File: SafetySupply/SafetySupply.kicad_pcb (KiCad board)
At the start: 2 copper layers, 30 x 60 mm, 48 parts, among them J1 Screw_Terminal_01x02, J2 Conn_01x01, J3 Screw_Terminal_01x02, J4 Conn_01x01, J5 Screw_Terminal_01x02, J6 Conn_01x01, J7 Conn_01x01, J8 Conn_01x01, J9 Conn_01x01, K1 FRM18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

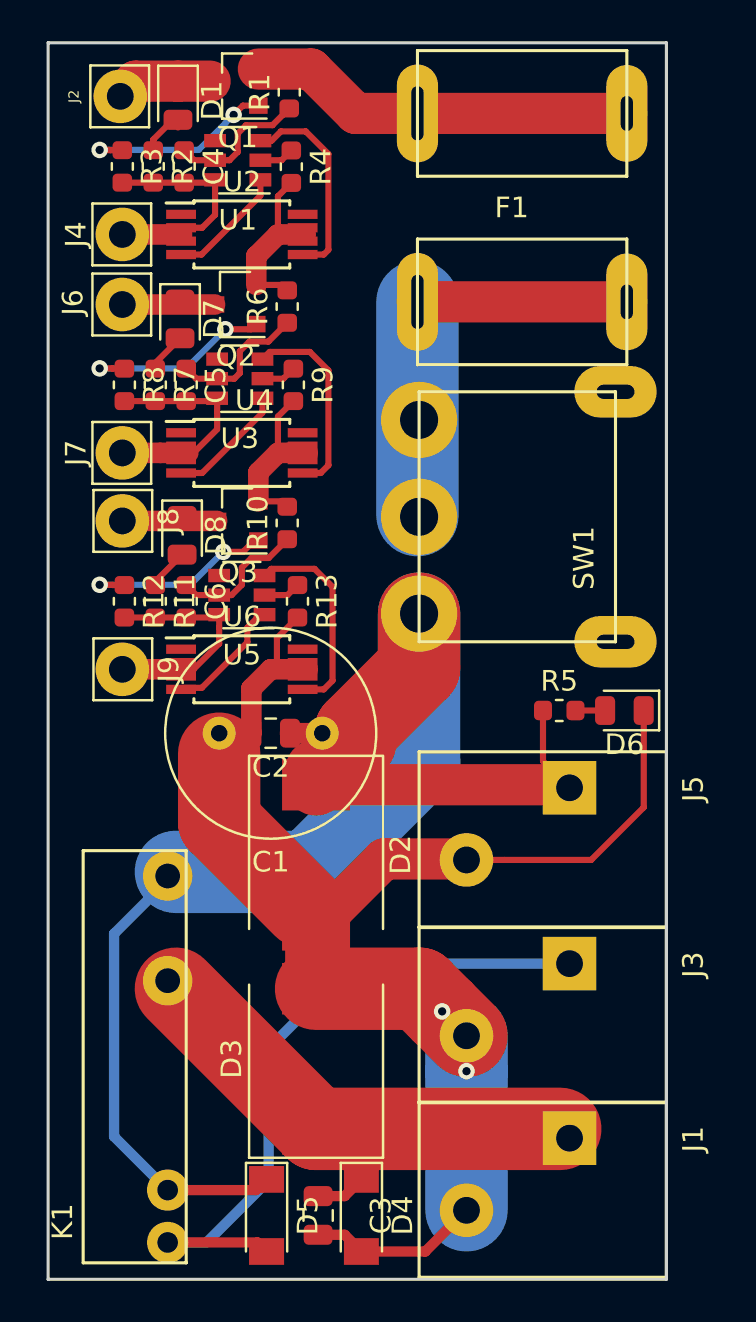
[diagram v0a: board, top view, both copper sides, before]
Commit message: Fixed silkscreen for SafetySupply, added mounting holes.
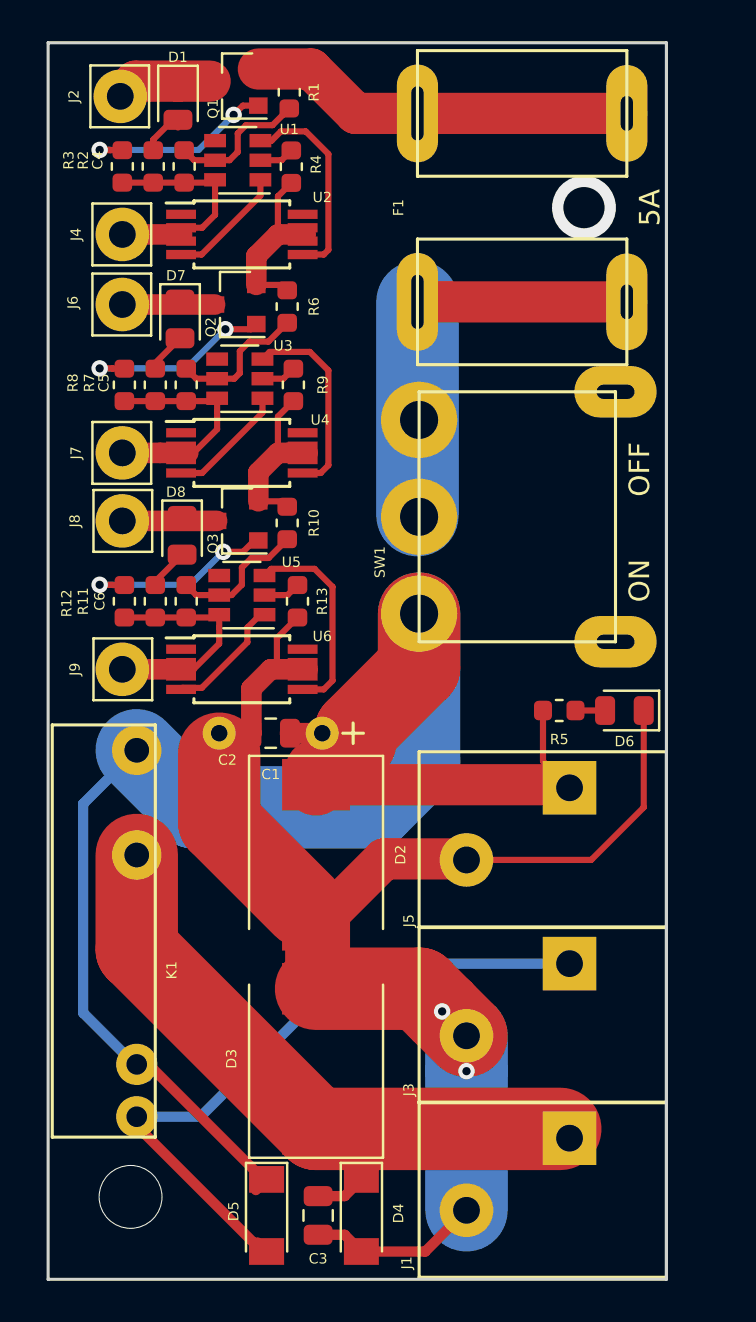
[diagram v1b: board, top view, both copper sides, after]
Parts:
- C1: footprint Capacitor_THT:C_Radial_D10.0mm_H20.0mm_P5.00mm -> Footprints:C_Radial_D10.0mm_H20.0mm_P5.00mm
- moved K1 6.28 mm to (138.2, 104.1)
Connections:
- SW1 pad 0: (no net) -> GND
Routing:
- net Net-(C3-Pad1): track 27.0 -> 34.2 mm
- net +12V: track 70.8 -> 76.4 mm
- net (no net): vias 0 -> 2
- added copper zone on B.Cu, net GND
- added copper zone on F.Cu, net GND
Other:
- board text added: "5A"
- board text added: "OFF"
- board text added: "ON"

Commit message: Added grouding vias in SafetySupply.
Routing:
- net GND: vias 2 -> 13
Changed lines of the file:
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@@
     (thickness 1.6)
     (drawings 7)
-    (tracks 226)
+    (tracks 237)
     (zones 0)
     (modules 48)
@@
   )
   (setup
-    (last_trace_width 0.5)
+    (last_trace_width 0.25)
     (user_trace_width 0.3)
     (user_trace_width 0.5)
@@
   (segment (start 153.018 106.9) (end 148 106.9) (width 4) (layer F.Cu) (net 7))
   (segment (start 155.3 110.9) (end 155.3 109.182) (width 4) (layer B.Cu) (net 7))
-  (via (at 155.3 110.9) (size 0.8) (drill 0.4) (layers F.Cu B.Cu) (net 7))
   (segment (start 154.118 108) (end 155.3 109.182) (width 4) (layer F.Cu) (net 7))
-  (via (at 154.118 108) (size 0.8) (drill 0.4) (layers F.Cu B.Cu) (net 7))
+  (via (at 162 118) (size 0.8) (drill 0.4) (layers F.Cu B.Cu) (net 7))
+  (via (at 162 110) (size 0.8) (drill 0.4) (layers F.Cu B.Cu) (net 7))
+  (via (at 162 102) (size 0.8) (drill 0.4) (layers F.Cu B.Cu) (net 7))
+  (via (at 162 86) (size 0.8) (drill 0.4) (layers F.Cu B.Cu) (net 7))
+  (via (at 162 81) (size 0.8) (drill 0.4) (layers F.Cu B.Cu) (net 7))
+  (via (at 157 69) (size 0.8) (drill 0.4) (layers F.Cu B.Cu) (net 7))
+  (via (at 151 69) (size 0.8) (drill 0.4) (layers F.Cu B.Cu) (net 7))
+  (via (at 137 68) (size 0.8) (drill 0.4) (layers F.Cu B.Cu) (net 7))
+  (via (at 137 79) (size 0.8) (drill 0.4) (layers F.Cu B.Cu) (net 7))
+  (via (at 137 89) (size 0.8) (drill 0.4) (layers F.Cu B.Cu) (net 7))
+  (via (at 144 104) (size 0.8) (drill 0.4) (layers F.Cu B.Cu) (net 7))
+  (via (at 142 119) (size 0.8) (drill 0.4) (layers F.Cu B.Cu) (net 7))
+  (via (at 137 114) (size 0.8) (drill 0.4) (layers F.Cu B.Cu) (net 7))
   (segment (start 146.6125 87.8) (end 145.5 87.8) (width 0.3) (layer F.Cu) (net 8))
   (segment (start 147.1 87.3125) (end 146.6125 87.8) (width 0.3) (layer F.Cu) (net 8))

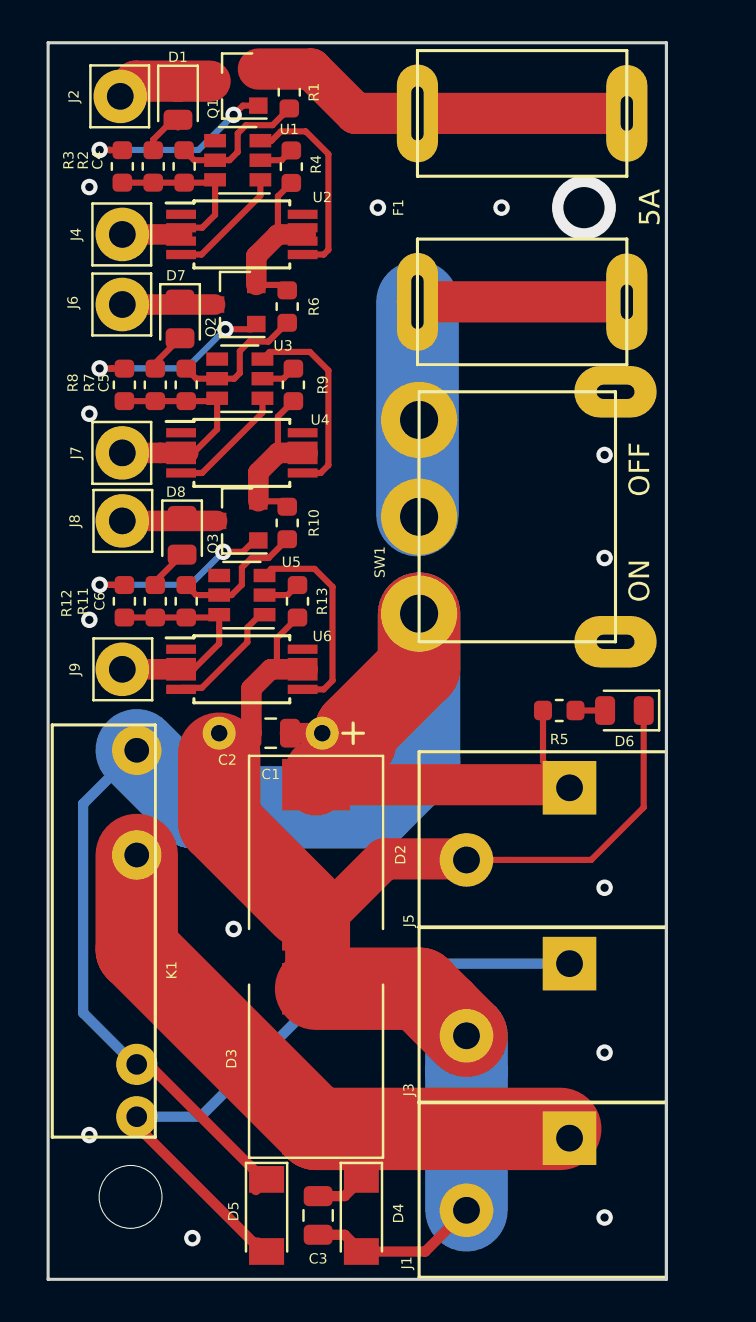
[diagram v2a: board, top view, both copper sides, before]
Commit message: First review. Fixed polygon pours, silkscreen and soldermask.
Squashed commit of the following:

commit 42a4a5d146683d2b2a8899b51cbc9eaef6797660
Author: Paweł <mackipawel@gmail.com>
Date:   Tue Apr 16 00:20:58 2019 +0200

    Changed solder mask design rules. Changed polygon pours clearence.

commit a27d25858da40b0edc55a62741cad58f571e73a1
Author: Paweł <mackipawel@gmail.com>
Date:   Sun Apr 14 15:00:25 2019 +0200

    Set via size to 0.3/0.6. Added silk screen descriptions in MotorDriver.

commit d55559f2128c74f860d75a89ad8b68139a6ba707
Author: Paweł <mackipawel@gmail.com>
Date:   Sun Apr 14 13:56:25 2019 +0200

    Added EcoTech logo in MotorController.
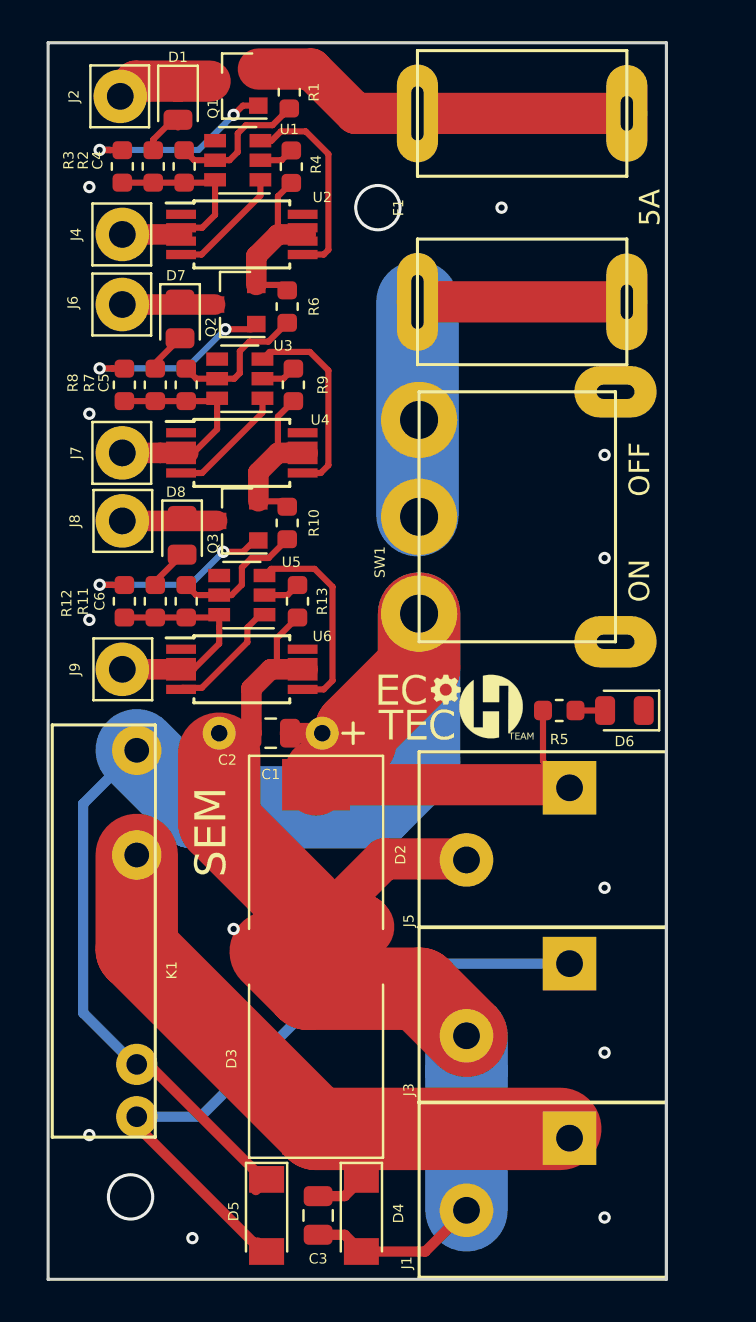
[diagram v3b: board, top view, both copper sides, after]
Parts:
- added G***: LOGO, Footprints:EcoTech_small, F.Cu at (154.6, 93.4)
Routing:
- net GND: track 71.0 -> 61.0 mm, vias 13 -> 12
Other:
- net class Default: via_dia 0.8 -> 0.6; via_drill 0.4 -> 0.3
- rule pad_to_mask_clearance: 0.051 -> 0.1
- rule solder_mask_min_width: 0.25 -> 0.2
- board text added: "SEM"

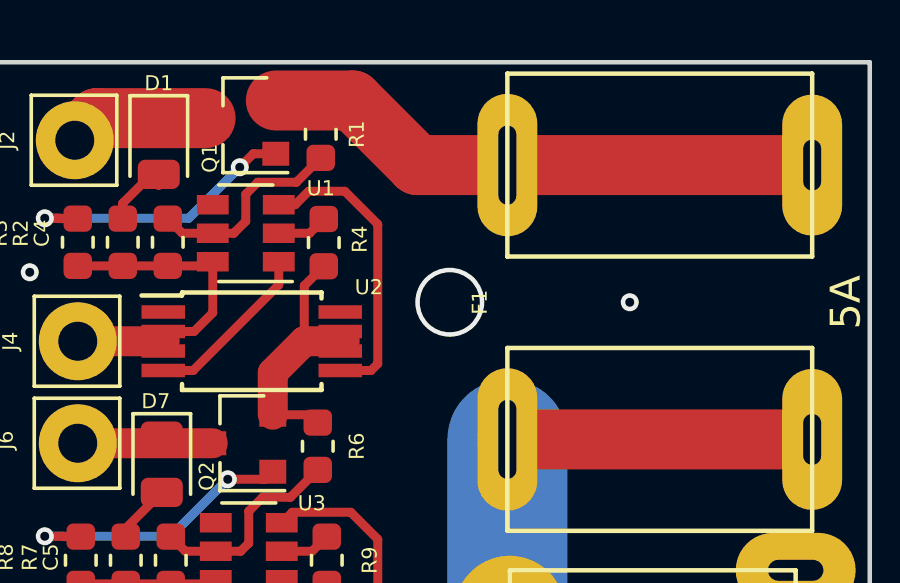
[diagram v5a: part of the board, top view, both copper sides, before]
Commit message: SafetySystem potentiometer.
Squashed commit of the following:

commit c85b31eae362b98e5e9037a9aad6a815148d0818
Author: Paweł <mackipawel@gmail.com>
Date:   Sun Apr 28 12:07:02 2019 +0200

    Added potentiometer to the SafetySysytem.
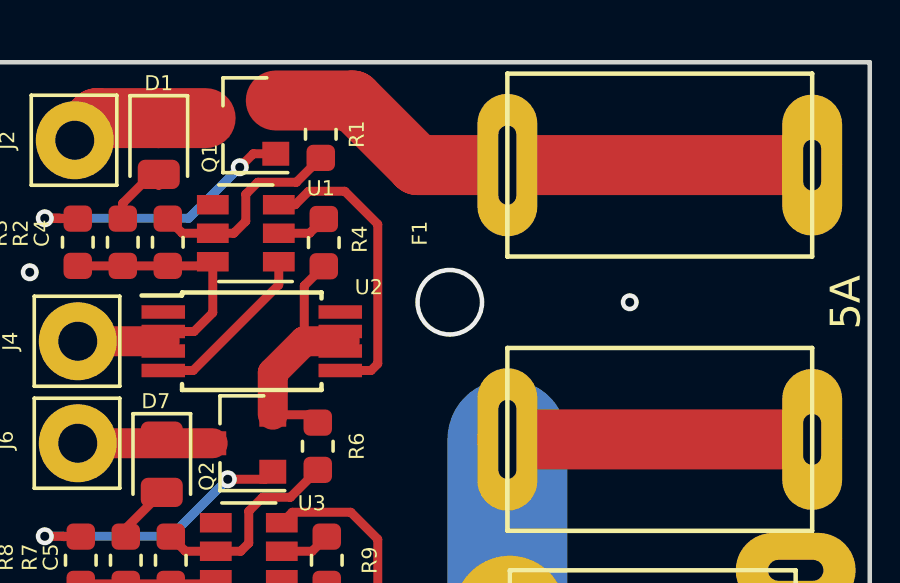
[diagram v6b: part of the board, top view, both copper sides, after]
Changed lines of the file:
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@@
   (module Footprints:Fuse_Blade_90 (layer F.Cu)
     (at 158 69 90)
-    (fp_text reference F1 (at 0 -6 270) (layer F.SilkS)
+    (fp_text reference F1 (at 2.3 -8 270) (layer F.SilkS)
       (effects (font (size 0.5 0.5) (thickness 0.1)))
     )
